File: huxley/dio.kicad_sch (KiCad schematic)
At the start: 1 part, among them J5 Conn_02x05_Counter_Clockwise

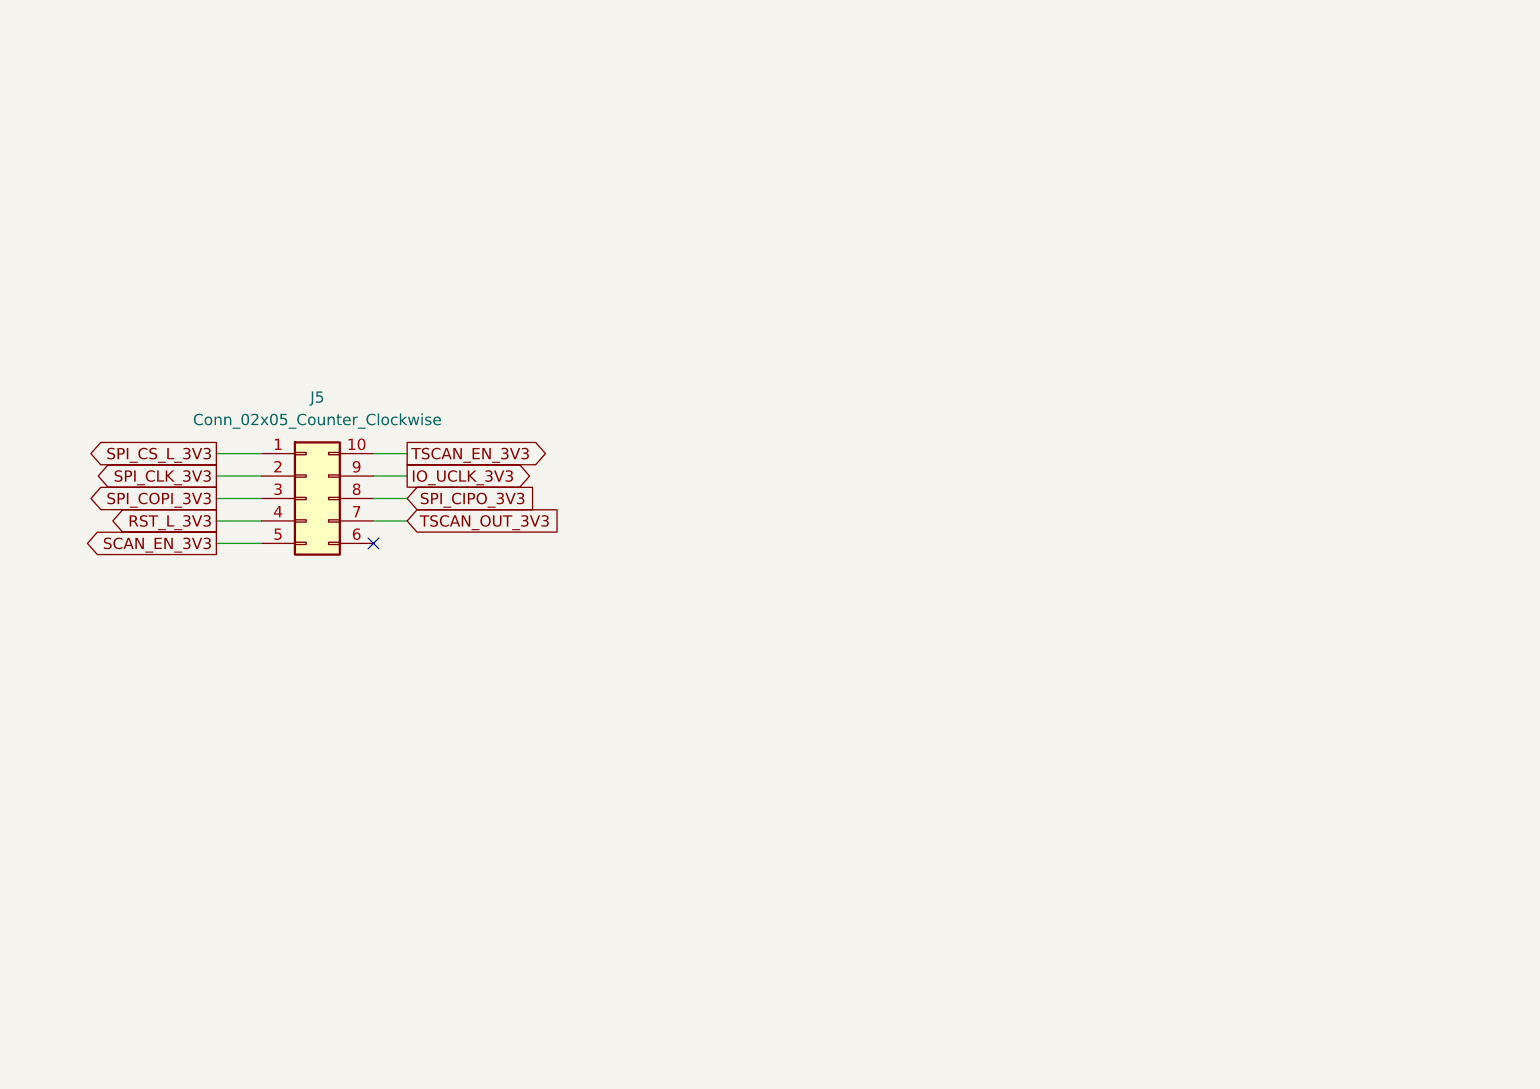
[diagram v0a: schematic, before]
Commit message: updated Ibias gen and footprints
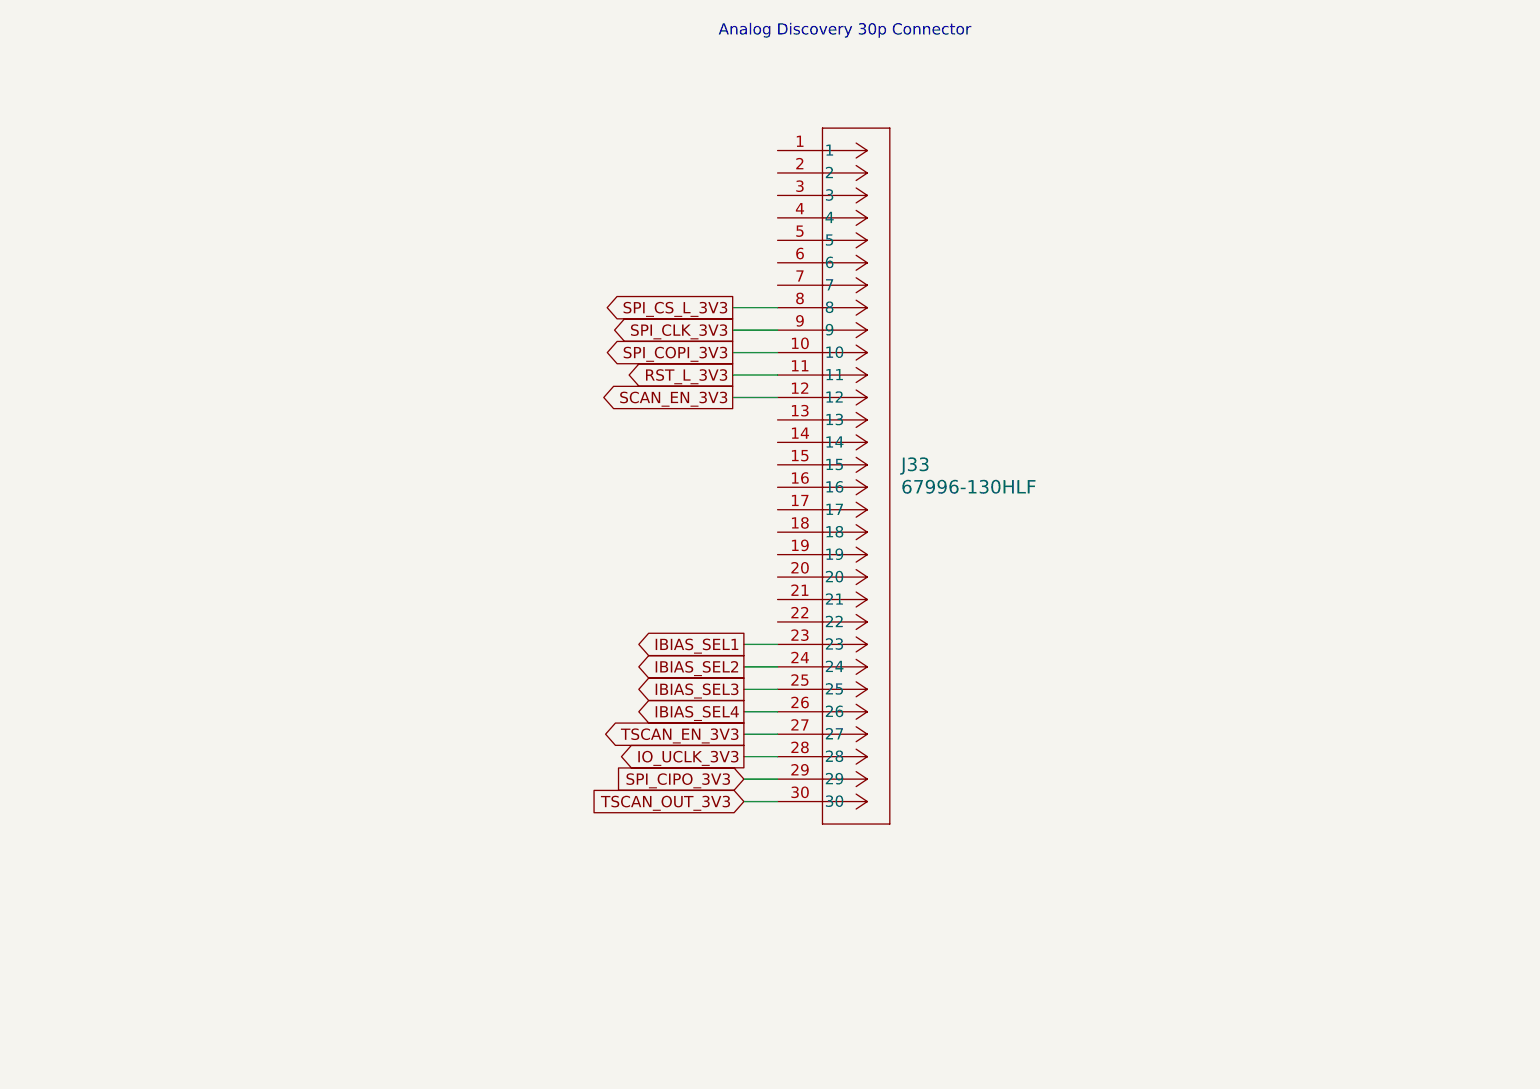
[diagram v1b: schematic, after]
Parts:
- removed J5: Conn_02x05_Counter_Clockwise, symbol Connector_Generic:Conn_02x05_Counter_Clockwise
- added J33: 67996-130HLF, 726_footprints:30p_connector, symbol _PHASE:67996-130HLF
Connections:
- net IO_UCLK_3V3: now also J33.28
- net RST_L_3V3: now also J33.11
- net SCAN_EN_3V3: now also J33.12
- net SPI_CIPO_3V3: now also J33.29
- net SPI_CLK_3V3: now also J33.9
- net SPI_COPI_3V3: now also J33.10
- net SPI_CS_L_3V3: now also J33.8
- net TSCAN_EN_3V3: now also J33.27
- net TSCAN_OUT_3V3: now also J33.30
- new net IBIAS_SEL1: J33.23
- new net IBIAS_SEL2: J33.24
- new net IBIAS_SEL3: J33.25
- new net IBIAS_SEL4: J33.26
- no-connect marks 1 -> 0
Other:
- note added: "Analog Discovery 30p Connector"

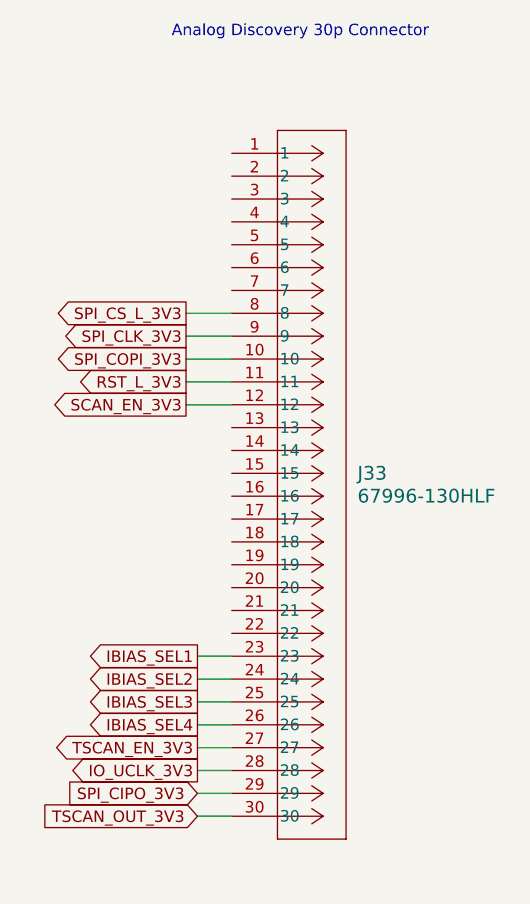
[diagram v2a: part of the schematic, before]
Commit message: added banana plugs and fixed analog discovery pinout
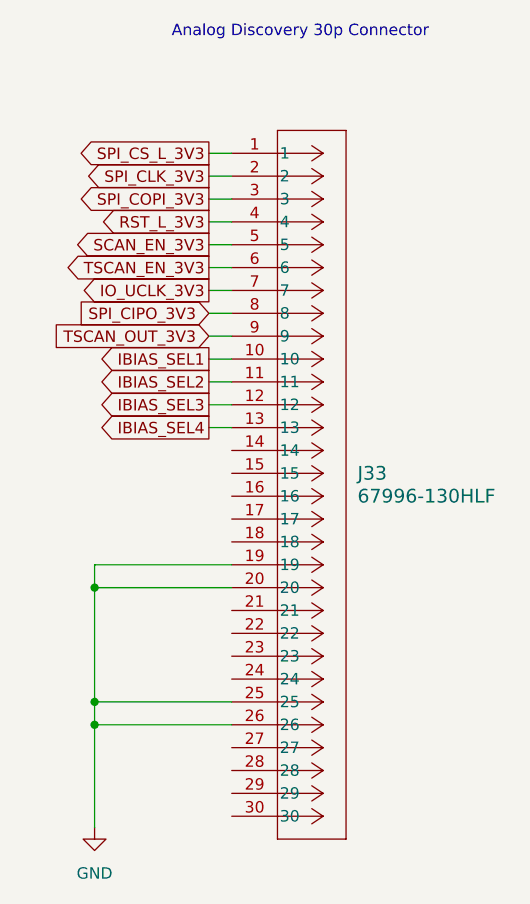
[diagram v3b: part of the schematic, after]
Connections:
- net IBIAS_SEL1: now also J33.10; no longer J33.23
- net IBIAS_SEL2: now also J33.11; no longer J33.24
- net IBIAS_SEL3: now also J33.12; no longer J33.25
- net IBIAS_SEL4: now also J33.13; no longer J33.26
- net IO_UCLK_3V3: now also J33.7; no longer J33.28
- net RST_L_3V3: now also J33.4; no longer J33.11
- net SCAN_EN_3V3: now also J33.5; no longer J33.12
- net SPI_CIPO_3V3: now also J33.8; no longer J33.29
- net SPI_CLK_3V3: now also J33.2; no longer J33.9
- net SPI_COPI_3V3: now also J33.3; no longer J33.10
- net SPI_CS_L_3V3: now also J33.1; no longer J33.8
- net TSCAN_EN_3V3: now also J33.6; no longer J33.27
- net TSCAN_OUT_3V3: now also J33.9; no longer J33.30
- net GND: now reaches J33.19
- net GND: now also J33.20, J33.25, J33.26

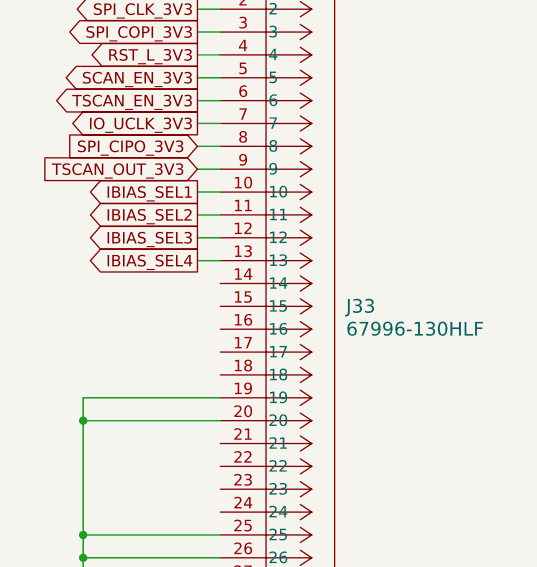
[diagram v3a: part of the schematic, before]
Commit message: reorganized pin assignment to level shifter; matched 3V3 power net name; minor schematic cleanup
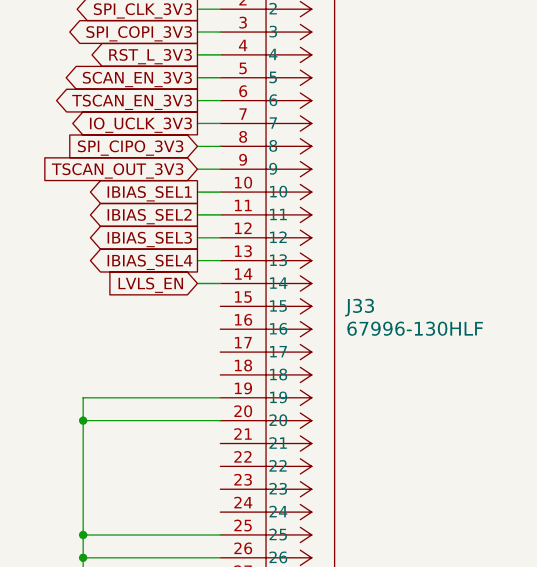
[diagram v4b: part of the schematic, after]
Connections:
- net LVLS_EN: now reaches J33.14
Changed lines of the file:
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@@
+	(wire
+		(pts
+			(xy 139.7 83.82) (xy 142.24 83.82)
+		)
+		(stroke
+			(width 0)
+			(type default)
+		)
+	)
 	(wire
 		(pts
@@
 				(hide yes)
 			)
+		)
+	)
+	(global_label "LVLS_EN"
+		(shape input)
+		(at 139.7 83.82 180)
+		(effects
+			(font
+				(size 1.27 1.27)
+			)
+			(justify right)
+		)
+		(property "Intersheetrefs" "${INTERSHEET_REFS}"
+			(at 139.7 83.82 0)
+			(effects
+				(font
+					(size 1.27 1.27)
+				)
+				(hide yes)
+			)

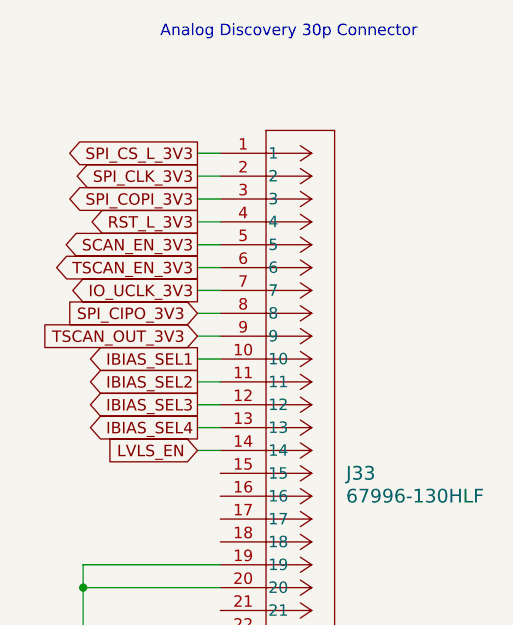
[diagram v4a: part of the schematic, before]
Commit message: quick remap of 30pin
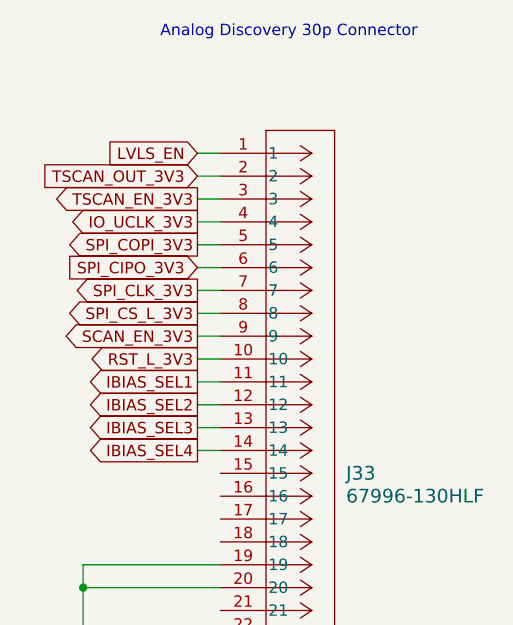
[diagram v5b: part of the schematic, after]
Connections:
- net IBIAS_SEL1: now also J33.11; no longer J33.10
- net IBIAS_SEL2: now also J33.12; no longer J33.11
- net IBIAS_SEL3: now also J33.13; no longer J33.12
- net IBIAS_SEL4: now also J33.14; no longer J33.13
- net IO_UCLK_3V3: now also J33.4; no longer J33.7
- net LVLS_EN: now also J33.1; no longer J33.14
- net RST_L_3V3: now also J33.10; no longer J33.4
- net SCAN_EN_3V3: now also J33.9; no longer J33.5
- net SPI_CIPO_3V3: now also J33.6; no longer J33.8
- net SPI_CLK_3V3: now also J33.7; no longer J33.2
- net SPI_COPI_3V3: now also J33.5; no longer J33.3
- net SPI_CS_L_3V3: now also J33.8; no longer J33.1
- net TSCAN_EN_3V3: now also J33.3; no longer J33.6
- net TSCAN_OUT_3V3: now also J33.2; no longer J33.9
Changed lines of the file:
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@@
+		)
+	)
+	(global_label "IBIAS_SEL4"
+		(shape output)
+		(at 139.7 83.82 180)
+		(fields_autoplaced yes)
+		(effects
+			(font
+				(size 1.27 1.27)
+			)
+			(justify right)
+		)
+		(property "Intersheetrefs" "${INTERSHEET_REFS}"
+			(at 126.3734 83.82 0)
+			(effects
+				(font
+					(size 1.27 1.27)
+				)
+				(justify right)
+				(hide yes)
+			)
+		)
+	)
+	(global_label "SPI_CS_L_3V3"
+		(shape output)
+		(at 139.7 68.58 180)
+		(effects
+			(font
+				(size 1.27 1.27)
+			)
+			(justify right)
+		)
+		(property "Intersheetrefs" "${INTERSHEET_REFS}"
+			(at 139.7 68.58 0)
+			(effects
+				(font
+					(size 1.27 1.27)
+				)
+				(hide yes)
+			)
+		)
+	)
+	(global_label "LVLS_EN"
+		(shape input)
+		(at 139.7 50.8 180)
+		(effects
+			(font
+				(size 1.27 1.27)
+			)
+			(justify right)
+		)
+		(property "Intersheetrefs" "${INTERSHEET_REFS}"
+			(at 139.7 50.8 0)
+			(effects
+				(font
+					(size 1.27 1.27)
+				)
+				(hide yes)
+			)
+		)
+	)
+	(global_label "SCAN_EN_3V3"
+		(shape output)
+		(at 139.7 71.12 180)
+		(effects
+			(font
+				(size 1.27 1.27)
+			)
+			(justify right)
+		)
+		(property "Intersheetrefs" "${INTERSHEET_REFS}"
+			(at 139.7 71.12 0)
+			(effects
+				(font
+					(size 1.27 1.27)
+				)
+				(hide yes)
+			)
 		)
 	)
 	(global_label "SPI_CIPO_3V3"
 		(shape input)
-		(at 139.7 68.58 180)
-		(effects
-			(font
-				(size 1.27 1.27)
-			)
-			(justify right)
-		)
-		(property "Intersheetrefs" "${INTERSHEET_REFS}"
-			(at 139.7 68.58 0)
-			(effects
-				(font
-					(size 1.27 1.27)
-				)
-				(hide yes)
-			)
-		)
-	)
-	(global_label "SPI_CS_L_3V3"
-		(shape output)
-		(at 139.7 50.8 180)
-		(effects
-			(font
-				(size 1.27 1.27)
-			)
-			(justify right)
-		)
-		(property "Intersheetrefs" "${INTERSHEET_REFS}"
-			(at 139.7 50.8 0)
-			(effects
-				(font
-					(size 1.27 1.27)
-				)
-				(hide yes)
-			)
-		)
-	)
-	(global_label "IBIAS_SEL2"
-		(shape output)
-		(at 139.7 76.2 180)
-		(fields_autoplaced yes)
-		(effects
-			(font
-				(size 1.27 1.27)
-			)
-			(justify right)
-		)
-		(property "Intersheetrefs" "${INTERSHEET_REFS}"
-			(at 126.3734 76.2 0)
-			(effects
-				(font
-					(size 1.27 1.27)
-				)
-				(justify right)
-				(hide yes)
-			)
-		)
-	)
-	(global_label "TSCAN_EN_3V3"
-		(shape output)
 		(at 139.7 63.5 180)
 		(effects
@@
 		)
 	)
-	(global_label "IBIAS_SEL1"
+	(global_label "RST_L_3V3"
 		(shape output)
 		(at 139.7 73.66 180)
-		(fields_autoplaced yes)
-		(effects
-			(font
-				(size 1.27 1.27)
-			)
-			(justify right)
-		)
-		(property "Intersheetrefs" "${INTERSHEET_REFS}"
-			(at 126.3734 73.66 0)
-			(effects
-				(font
-					(size 1.27 1.27)
-				)
-				(justify right)
-				(hide yes)
-			)
-		)
-	)
-	(global_label "IO_UCLK_3V3"
-		(shape output)
-		(at 139.7 66.04 180)
-		(effects
-			(font
-				(size 1.27 1.27)
-			)
-			(justify right)
-		)
-		(property "Intersheetrefs" "${INTERSHEET_REFS}"
-			(at 139.7 66.04 0)
-			(effects
-				(font
-					(size 1.27 1.27)
-				)
-				(hide yes)
-			)
-		)
-	)
-	(global_label "SPI_CLK_3V3"
-		(shape output)
-		(at 139.7 53.34 180)
-		(effects
-			(font
-				(size 1.27 1.27)
-			)
-			(justify right)
-		)
-		(property "Intersheetrefs" "${INTERSHEET_REFS}"
-			(at 139.7 53.34 0)
-			(effects
-				(font
-					(size 1.27 1.27)
-				)
-				(hide yes)
-			)
-		)
-	)
-	(global_label "SPI_COPI_3V3"
-		(shape output)
-		(at 139.7 55.88 180)
-		(effects
-			(font
-				(size 1.27 1.27)
-			)
-			(justify right)
-		)
-		(property "Intersheetrefs" "${INTERSHEET_REFS}"
-			(at 139.7 55.88 0)
+		(effects
+			(font
+				(size 1.27 1.27)
+			)
+			(justify right)
+		)
+		(property "Intersheetrefs" "${INTERSHEET_REFS}"
+			(at 139.7 73.66 0)
 			(effects
 				(font
@@
 	(global_label "TSCAN_OUT_3V3"
 		(shape input)
-		(at 139.7 71.12 180)
-		(effects
-			(font
-				(size 1.27 1.27)
-			)
-			(justify right)
-		)
-		(property "Intersheetrefs" "${INTERSHEET_REFS}"
-			(at 139.7 71.12 0)
-			(effects
-				(font
-					(size 1.27 1.27)
-				)
-				(hide yes)
-			)
-		)
-	)
-	(global_label "RST_L_3V3"
+		(at 139.7 53.34 180)
+		(effects
+			(font
+				(size 1.27 1.27)
+			)
+			(justify right)
+		)
+		(property "Intersheetrefs" "${INTERSHEET_REFS}"
+			(at 139.7 53.34 0)
+			(effects
+				(font
+					(size 1.27 1.27)
+				)
+				(hide yes)
+			)
+		)
+	)
+	(global_label "IO_UCLK_3V3"
 		(shape output)
 		(at 139.7 58.42 180)
@@
 		)
 	)
-	(global_label "IBIAS_SEL4"
+	(global_label "TSCAN_EN_3V3"
+		(shape output)
+		(at 139.7 55.88 180)
+		(effects
+			(font
+				(size 1.27 1.27)
+			)
+			(justify right)
+		)
+		(property "Intersheetrefs" "${INTERSHEET_REFS}"
+			(at 139.7 55.88 0)
+			(effects
+				(font
+					(size 1.27 1.27)
+				)
+				(hide yes)
+			)
+		)
+	)
+	(global_label "SPI_CLK_3V3"
+		(shape output)
+		(at 139.7 66.04 180)
+		(effects
+			(font
+				(size 1.27 1.27)
+			)
+			(justify right)
+		)
+		(property "Intersheetrefs" "${INTERSHEET_REFS}"
+			(at 139.7 66.04 0)
+			(effects
+				(font
+					(size 1.27 1.27)
+				)
+				(hide yes)
+			)
+		)
+	)
+	(global_label "IBIAS_SEL3"
 		(shape output)
 		(at 139.7 81.28 180)
@@
 		)
 	)
-	(global_label "IBIAS_SEL3"
+	(global_label "IBIAS_SEL2"
 		(shape output)
 		(at 139.7 78.74 180)
@@
 		)
 	)
-	(global_label "LVLS_EN"
-		(shape input)
-		(at 139.7 83.82 180)
-		(effects
-			(font
-				(size 1.27 1.27)
-			)
-			(justify right)
-		)
-		(property "Intersheetrefs" "${INTERSHEET_REFS}"
-			(at 139.7 83.82 0)
-			(effects
-				(font
-					(size 1.27 1.27)
-				)
-				(hide yes)
-			)
-		)
-	)
-	(global_label "SCAN_EN_3V3"
+	(global_label "IBIAS_SEL1"
+		(shape output)
+		(at 139.7 76.2 180)
+		(fields_autoplaced yes)
+		(effects
+			(font
+				(size 1.27 1.27)
+			)
+			(justify right)
+		)
+		(property "Intersheetrefs" "${INTERSHEET_REFS}"
+			(at 126.3734 76.2 0)
+			(effects
+				(font
+					(size 1.27 1.27)
+				)
+				(justify right)
+				(hide yes)
+			)
+		)
+	)
+	(global_label "SPI_COPI_3V3"
 		(shape output)
 		(at 139.7 60.96 180)
